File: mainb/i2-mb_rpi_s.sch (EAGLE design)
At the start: 30 parts, among them IC3 DS1307Z, T1 BC337, T2 BC337, X1 MICROMATCH-4, X15 C-GRID-03-70543, X2 MICROMATCH-4, X3 MICROMATCH-4, X8 MICROMATCH-4, X9 eth (mb->rpi)

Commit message: zmieniony ksztalt mainb
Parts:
- removed X1, X2, X3, X8: MICROMATCH-4, con-maritex:MICROMATCH-4
- removed X12, X13, X14: (no value), con-ptr500:AK500/3-H
- removed X4, X5, X6: (no value), con-ptr500:AK500/3
- added I2C_1, I2C_2, I2C_3, I2C_4: C-GRID-03-70553, con-molex:C-GRID-03-70553
- added PWR1, PWR2, PWR3: TBMP5103RC-KFV1, con-maritex:TBMP5103RC-KFV1
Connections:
- net +12V_OUT: now also PWR1-3.P, PWR2-3.P, PWR3-3.P; no longer X4-3.KL, X5-3.KL, X6-3.KL
- net +5V: now also PWR1-1.P, PWR2-1.P, PWR3-1.P; no longer X4-1.KL, X5-1.KL, X6-1.KL
- net GND: now also I2C_1-3.S, I2C_2-3.S, I2C_3-3.S, I2C_4-3.S, PWR1-2.P, PWR2-2.P, PWR3-2.P; no longer X1-4.S, X12-2.KL, X13-2.KL, X14-2.KL, X2-4.S, X3-4.S, X4-2.KL, X5-2.KL, X6-2.KL, X8-4.S
- net SCL: now also I2C_1-2.S, I2C_2-2.S, I2C_3-2.S, I2C_4-2.S; no longer X1-3.S, X2-3.S, X3-3.S, X8-3.S
- net SDA: now also I2C_1-1.S, I2C_2-1.S, I2C_3-1.S, I2C_4-1.S; no longer X1-2.S, X2-2.S, X3-2.S, X8-2.S

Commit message: 21.11.13 23:39
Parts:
- I2C_1: value C-GRID-03-70553 -> C-GRID-03-70543; device con-molex:C-GRID-03-70553 -> con-molex:C-GRID-03-70543; OC_FARNELL (none) -> unknown; OC_NEWARK (none) -> unknown
- renumbered X15 to PWR4
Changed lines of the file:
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@@
 <?xml version="1.0" encoding="utf-8"?>
 <!DOCTYPE eagle SYSTEM "eagle.dtd">
-<eagle version="6.4">
+<eagle version="6.1">
 <drawing>
 <settings>
@@
 <part name="SUPPLY2" library="supply2" deviceset="+5V/1" device="" value="+5V_RPI"/>
 <part name="SUPPLY3" library="supply2" deviceset="+5V/1" device="" value="+5V_RPI"/>
-<part name="X15" library="con-molex" deviceset="C-GRID-03" device="-70543"/>
+<part name="PWR4" library="con-molex" deviceset="C-GRID-03" device="-70543"/>
 <part name="SUPPLY1" library="supply2" deviceset="+12V" device="" value="+12V_OUT"/>
 <part name="GND1" library="supply1" deviceset="GND" device=""/>
 <part name="T1" library="transistor" deviceset="BC337" device=""/>
 <part name="T2" library="transistor" deviceset="BC337" device=""/>
-<part name="I2C_1" library="con-molex" deviceset="C-GRID-03" device="-70553"/>
 <part name="I2C_2" library="con-molex" deviceset="C-GRID-03" device="-70553"/>
 <part name="I2C_3" library="con-molex" deviceset="C-GRID-03" device="-70553"/>
@@
 <part name="PWR2" library="con-maritex" deviceset="TBMP5103RC-KF" device="V1"/>
 <part name="PWR3" library="con-maritex" deviceset="TBMP5103RC-KF" device="V1"/>
+<part name="I2C_1" library="con-molex" deviceset="C-GRID-03" device="-70543">
+<attribute name="MF" value=""/>
+<attribute name="MPN" value=""/>
+<attribute name="OC_FARNELL" value="unknown"/>
+<attribute name="OC_NEWARK" value="unknown"/>
+</part>
 </parts>
 <sheets>
@@
 <attribute name="VALUE" x="27.813" y="-44.831" size="1.778" layer="96"/>
 </instance>
-<instance part="X15" gate="-1" x="48.26" y="-2.54" smashed="yes" rot="R180">
+<instance part="PWR4" gate="-1" x="48.26" y="-2.54" smashed="yes" rot="R180">
 <attribute name="NAME" x="45.72" y="-1.778" size="1.524" layer="95" rot="R180"/>
 </instance>
-<instance part="X15" gate="-2" x="48.26" y="-15.24" rot="R180"/>
-<instance part="X15" gate="-3" x="48.26" y="25.4" rot="R180"/>
+<instance part="PWR4" gate="-2" x="48.26" y="-15.24" rot="R180"/>
+<instance part="PWR4" gate="-3" x="48.26" y="25.4" rot="R180"/>
 <instance part="SUPPLY1" gate="+12V" x="-63.5" y="25.4" smashed="yes">
 <attribute name="VALUE" x="-68.58" y="28.575" size="1.778" layer="96"/>
@@
 <instance part="T1" gate="G$1" x="-71.12" y="-12.7"/>
 <instance part="T2" gate="G$1" x="10.16" y="-15.24"/>
-<instance part="I2C_1" gate="-1" x="60.96" y="-55.88" smashed="yes">
-<attribute name="NAME" x="63.5" y="-56.642" size="1.524" layer="95"/>
-</instance>
-<instance part="I2C_1" gate="-2" x="60.96" y="-68.58"/>
-<instance part="I2C_1" gate="-3" x="60.96" y="-83.82"/>
 <instance part="I2C_2" gate="-1" x="60.96" y="-58.42" smashed="yes">
 <attribute name="NAME" x="63.5" y="-59.182" size="1.524" layer="95"/>
@@
 <instance part="PWR3" gate="-2" x="60.96" y="-22.86" rot="MR0"/>
 <instance part="PWR3" gate="-3" x="60.96" y="27.94" rot="MR0"/>
+<instance part="I2C_1" gate="-1" x="60.96" y="-55.88" smashed="yes">
+<attribute name="NAME" x="63.5" y="-56.642" size="1.524" layer="95"/>
+</instance>
+<instance part="I2C_1" gate="-2" x="60.96" y="-68.58"/>
+<instance part="I2C_1" gate="-3" x="60.96" y="-83.82"/>
 </instances>
 <busses>
@@
 <junction x="55.88" y="-73.66"/>
 <label x="49.53" y="-68.326" size="1.778" layer="95"/>
-<pinref part="I2C_1" gate="-2" pin="S"/>
 <pinref part="I2C_2" gate="-2" pin="S"/>
 <pinref part="I2C_3" gate="-2" pin="S"/>
 <pinref part="I2C_4" gate="-2" pin="S"/>
+<pinref part="I2C_1" gate="-2" pin="S"/>
 </segment>
 <segment>
@@
 <junction x="55.88" y="-60.96"/>
 <label x="49.276" y="-55.626" size="1.778" layer="95"/>
-<pinref part="I2C_1" gate="-1" pin="S"/>
 <pinref part="I2C_2" gate="-1" pin="S"/>
 <pinref part="I2C_3" gate="-1" pin="S"/>
 <pinref part="I2C_4" gate="-1" pin="S"/>
+<pinref part="I2C_1" gate="-1" pin="S"/>
 </segment>
 <segment>
@@
 <pinref part="SUPPLY7" gate="+5V" pin="+5V"/>
 <wire x1="53.34" y1="7.62" x2="53.34" y2="5.08" width="0.1524" layer="91"/>
-<pinref part="X15" gate="-1" pin="S"/>
+<pinref part="PWR4" gate="-1" pin="S"/>
 <wire x1="53.34" y1="5.08" x2="53.34" y2="2.54" width="0.1524" layer="91"/>
 <wire x1="53.34" y1="2.54" x2="53.34" y2="0" width="0.1524" layer="91"/>
@@
 <segment>
 <pinref part="GND11" gate="1" pin="GND"/>
-<pinref part="X15" gate="-2" pin="S"/>
+<pinref part="PWR4" gate="-2" pin="S"/>
 <wire x1="50.8" y1="-15.24" x2="53.34" y2="-15.24" width="0.1524" layer="91"/>
 <wire x1="53.34" y1="-15.24" x2="53.34" y2="-17.78" width="0.1524" layer="91"/>
@@
 <junction x="55.88" y="-88.9"/>
 <junction x="55.88" y="-91.44"/>
-<pinref part="I2C_1" gate="-3" pin="S"/>
 <pinref part="I2C_2" gate="-3" pin="S"/>
 <pinref part="I2C_3" gate="-3" pin="S"/>
 <pinref part="I2C_4" gate="-3" pin="S"/>
+<pinref part="I2C_1" gate="-3" pin="S"/>
 </segment>
 <segment>
@@
 <pinref part="SUPPLY6" gate="+12V" pin="+12V"/>
 <wire x1="53.34" y1="35.56" x2="53.34" y2="33.02" width="0.1524" layer="91"/>
-<pinref part="X15" gate="-3" pin="S"/>
+<pinref part="PWR4" gate="-3" pin="S"/>
 <wire x1="53.34" y1="33.02" x2="53.34" y2="30.48" width="0.1524" layer="91"/>
 <wire x1="53.34" y1="30.48" x2="53.34" y2="27.94" width="0.1524" layer="91"/>

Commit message: 26.11 10:46
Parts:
- added C1: 100n, rcl:C-EUC0603
- added LED1, LED2, LED3: LED0603, wb:LED0603
- added R4, R5, R6: 500, rcl:R-EU_R0603
- added R7: (no value), rcl:R-EU_R0603
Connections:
- new net LED2: LED2.C, U$2.GPIO23
- new net LED3: LED3.C, U$2.GPIO24
- new net N$10: IC3.SQW, R7.2
- new net N$4: LED2.A, R5.1
- new net N$5: LED1.A, R4.1
- new net N$7: LED1.C, U$2.GPIO25
- new net N$8: LED3.A, R6.1
- net +5V_RPI: now also C1.1, R4.2, R5.2, R6.2, R7.1
- net GND: now also C1.2
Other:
- note removed: "AKU-"
- moved on the sheet: BAT, I2C_1-1, I2C_1-2, I2C_1-3, I2C_2-1, I2C_2-2, I2C_2-3, I2C_3-1, I2C_3-2, I2C_3-3, I2C_4-1, I2C_4-2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

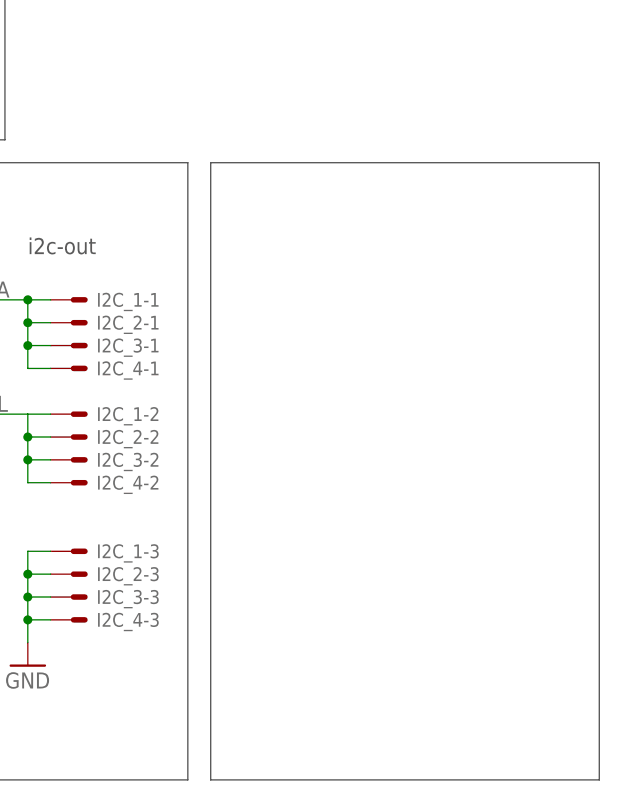
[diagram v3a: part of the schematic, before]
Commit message: RPi camera board added and library, added servos.lbr
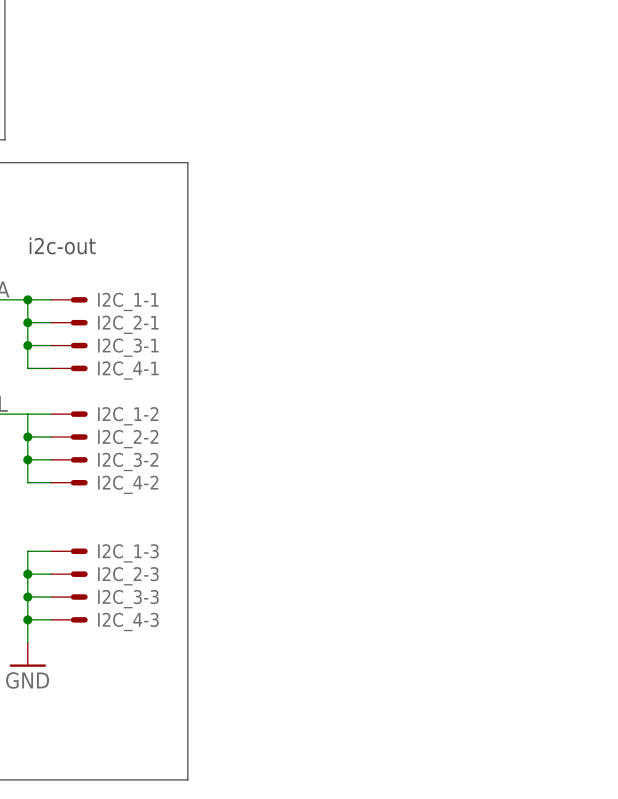
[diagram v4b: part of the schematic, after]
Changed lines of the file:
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@@
 <circle x="-157.48" y="-10.16" radius="2.54" width="1.4224" layer="94"/>
 <text x="-170.18" y="-10.16" size="2.54" layer="97">AKU+</text>
-<wire x1="96.52" y1="-109.22" x2="96.52" y2="-40.64" width="0.1524" layer="97"/>
-<wire x1="139.7" y1="-109.22" x2="139.7" y2="-40.64" width="0.1524" layer="97"/>
-<wire x1="96.52" y1="-109.22" x2="139.7" y2="-109.22" width="0.1524" layer="97"/>
-<wire x1="96.52" y1="-40.64" x2="139.7" y2="-40.64" width="0.1524" layer="97"/>
 </plain>
 <instances>

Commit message: 03-12-13 20:52
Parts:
- I2C_1: value C-GRID-03-70543 -> MICROMATCH-4; device con-molex:C-GRID-03-70543 -> con-amp-micromatch:MICROMATCH-4; OC_FARNELL unknown -> (none); OC_NEWARK unknown -> (none)
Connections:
- net +5V: now also I2C_1-4.S
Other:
- moved on the sheet: R28, R3, T1, T2, U$8, X9-1, X9-2, X9-3, X9-4, X9-5, X9-6, X9-7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

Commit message: 11.12.13 18:50
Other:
- note removed: "i2c-out"
- moved on the sheet: BAT, I2C_1-1, I2C_1-2, I2C_1-3, I2C_1-4, I2C_2-1, I2C_2-2, I2C_2-3, I2C_3-1, I2C_3-2, I2C_3-3, I2C_4-1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

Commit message: misc changes
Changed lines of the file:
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@@
 <?xml version="1.0" encoding="utf-8"?>
 <!DOCTYPE eagle SYSTEM "eagle.dtd">
-<eagle version="6.1">
+<eagle version="6.4">
 <drawing>
 <settings>
@@
 <part name="I2C_1" library="con-amp-micromatch" deviceset="MICROMATCH-4" device=""/>
 <part name="SUPPLY5" library="supply2" deviceset="+5V" device="" value="+5V_OUT"/>
+<part name="GND1" library="supply1" deviceset="GND" device=""/>
 </parts>
 <sheets>
@@
 <attribute name="VALUE" x="41.275" y="3.175" size="1.778" layer="96"/>
 </instance>
+<instance part="GND1" gate="1" x="40.64" y="-38.1"/>
 </instances>
 <busses>
@@
 <wire x1="-38.1" y1="-40.64" x2="-38.1" y2="-106.68" width="0.762" layer="92"/>
 <wire x1="12.7" y1="5.08" x2="12.7" y2="-40.64" width="0.762" layer="92"/>
-<wire x1="-38.1" y1="-106.68" x2="-12.7" y2="-106.68" width="0.762" layer="92"/>
+<wire x1="-38.1" y1="-106.68" x2="-17.78" y2="-106.68" width="0.762" layer="92"/>
 </segment>
 </bus>
@@
 </segment>
 <segment>
+<pinref part="I2C_4" gate="-2" pin="S"/>
+<wire x1="-20.32" y1="-119.38" x2="-20.32" y2="-106.68" width="0.1524" layer="91"/>
+</segment>
+<segment>
 <wire x1="12.7" y1="-5.08" x2="15.24" y2="-7.62" width="0.1524" layer="91"/>
 <wire x1="15.24" y1="-7.62" x2="38.1" y2="-7.62" width="0.1524" layer="91"/>
 <wire x1="38.1" y1="-7.62" x2="45.72" y2="-7.62" width="0.1524" layer="91"/>
-<wire x1="-20.32" y1="-119.38" x2="-20.32" y2="-111.76" width="0.1524" layer="91"/>
-<wire x1="-20.32" y1="-111.76" x2="38.1" y2="-30.48" width="0.1524" layer="91"/>
 <wire x1="38.1" y1="-30.48" x2="38.1" y2="-20.32" width="0.1524" layer="91"/>
 <wire x1="38.1" y1="-20.32" x2="38.1" y2="-7.62" width="0.1524" layer="91"/>
@@
 <wire x1="45.72" y1="-20.32" x2="38.1" y2="-20.32" width="0.1524" layer="91"/>
 <junction x="38.1" y="-20.32"/>
-<junction x="38.1" y="-30.48"/>
 <label x="21.59" y="-7.366" size="1.778" layer="95"/>
 <pinref part="I2C_2" gate="-2" pin="S"/>
 <pinref part="I2C_3" gate="-2" pin="S"/>
-<pinref part="I2C_4" gate="-2" pin="S"/>
 <pinref part="I2C_1" gate="-2" pin="S"/>
 </segment>
@@
 </segment>
 <segment>
+<pinref part="I2C_4" gate="-1" pin="S"/>
+<wire x1="-17.78" y1="-119.38" x2="-17.78" y2="-106.68" width="0.1524" layer="91"/>
+</segment>
+<segment>
 <wire x1="12.7" y1="-2.54" x2="15.24" y2="-5.08" width="0.1524" layer="91"/>
 <wire x1="15.24" y1="-5.08" x2="35.56" y2="-5.08" width="0.1524" layer="91"/>
 <wire x1="35.56" y1="-5.08" x2="45.72" y2="-5.08" width="0.1524" layer="91"/>
-<wire x1="-17.78" y1="-119.38" x2="-17.78" y2="-109.22" width="0.1524" layer="91"/>
 <wire x1="45.72" y1="-27.94" x2="35.56" y2="-27.94" width="0.1524" layer="91"/>
-<wire x1="-17.78" y1="-109.22" x2="35.56" y2="-27.94" width="0.1524" layer="91"/>
 <wire x1="45.72" y1="-17.78" x2="35.56" y2="-17.78" width="0.1524" layer="91"/>
 <wire x1="35.56" y1="-27.94" x2="35.56" y2="-17.78" width="0.1524" layer="91"/>
@@
 <junction x="35.56" y="-5.08"/>
 <junction x="35.56" y="-17.78"/>
-<junction x="35.56" y="-27.94"/>
 <label x="21.336" y="-4.826" size="1.778" layer="95"/>
 <pinref part="I2C_2" gate="-1" pin="S"/>
 <pinref part="I2C_3" gate="-1" pin="S"/>
-<pinref part="I2C_4" gate="-1" pin="S"/>
 <pinref part="I2C_1" gate="-1" pin="S"/>
 </segment>
@@
 </segment>
 <segment>
-<wire x1="45.72" y1="-33.02" x2="40.64" y2="-33.02" width="0.1524" layer="91"/>
-<wire x1="45.72" y1="-10.16" x2="40.64" y2="-10.16" width="0.1524" layer="91"/>
-<wire x1="40.64" y1="-10.16" x2="40.64" y2="-22.86" width="0.1524" layer="91"/>
-<wire x1="40.64" y1="-22.86" x2="40.64" y2="-33.02" width="0.1524" layer="91"/>
+<pinref part="GND12" gate="1" pin="GND"/>
+<pinref part="I2C_4" gate="-3" pin="S"/>
 <wire x1="-22.86" y1="-119.38" x2="-22.86" y2="-114.3" width="0.1524" layer="91"/>
-<wire x1="40.64" y1="-33.02" x2="-22.86" y2="-114.3" width="0.1524" layer="91"/>
-<pinref part="GND12" gate="1" pin="GND"/>
 <wire x1="-22.86" y1="-114.3" x2="-27.94" y2="-114.3" width="0.1524" layer="91"/>
-<wire x1="45.72" y1="-22.86" x2="40.64" y2="-22.86" width="0.1524" layer="91"/>
-<junction x="40.64" y="-22.86"/>
-<junction x="40.64" y="-33.02"/>
-<junction x="-22.86" y="-114.3"/>
-<pinref part="I2C_2" gate="-3" pin="S"/>
-<pinref part="I2C_3" gate="-3" pin="S"/>
-<pinref part="I2C_4" gate="-3" pin="S"/>
-<pinref part="I2C_1" gate="-3" pin="S"/>
 </segment>
 <segment>
@@
 <pinref part="GND14" gate="1" pin="GND"/>
 </segment>
-</net>
+<segment>
+<wire x1="45.72" y1="-33.02" x2="40.64" y2="-33.02" width="0.1524" layer="91"/>
+<wire x1="45.72" y1="-10.16" x2="40.64" y2="-10.16" width="0.1524" layer="91"/>
+<wire x1="40.64" y1="-10.16" x2="40.64" y2="-22.86" width="0.1524" layer="91"/>
+<wire x1="40.64" y1="-22.86" x2="40.64" y2="-33.02" width="0.1524" layer="91"/>
+<wire x1="45.72" y1="-22.86" x2="40.64" y2="-22.86" width="0.1524" layer="91"/>
+<junction x="40.64" y="-22.86"/>
+<pinref part="I2C_2" gate="-3" pin="S"/>
+<pinref part="I2C_3" gate="-3" pin="S"/>
+<pinref part="I2C_1" gate="-3" pin="S"/>
+<pinref part="GND1" gate="1" pin="GND"/>
+<wire x1="40.64" y1="-33.02" x2="40.64" y2="-35.56" width="0.1524" layer="91"/>
+<junction x="40.64" y="-33.02"/>
+</segment>
+</net>

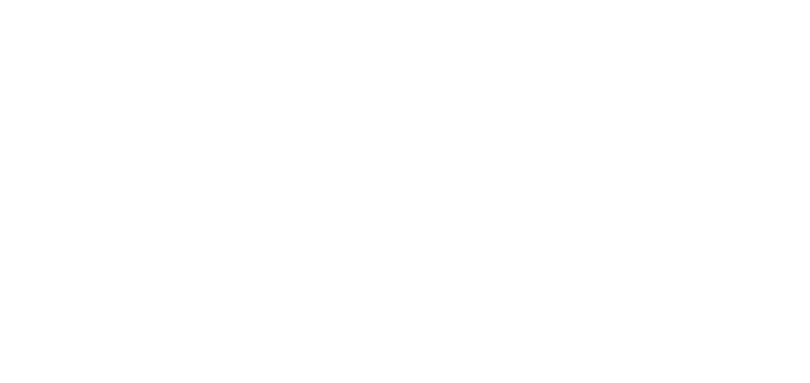
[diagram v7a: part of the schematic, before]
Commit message: /mainb: 1) pins on relays
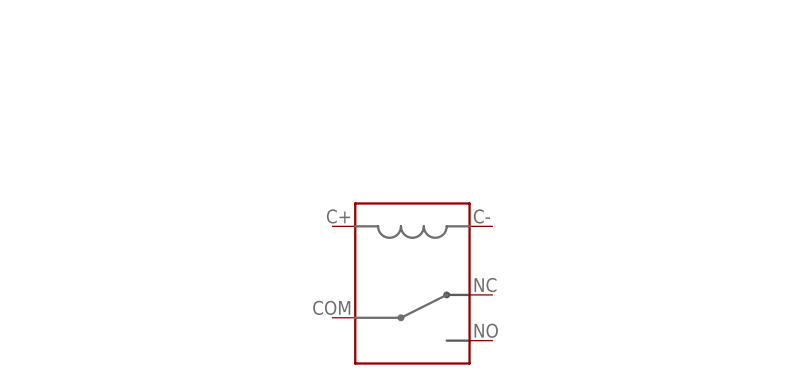
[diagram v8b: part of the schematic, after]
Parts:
- added U$9: FBR51, wb:FBR51
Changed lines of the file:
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@@
 <?xml version="1.0" encoding="utf-8"?>
 <!DOCTYPE eagle SYSTEM "eagle.dtd">
-<eagle version="6.4">
+<eagle version="6.5.0">
 <drawing>
 <settings>
@@
 <part name="SUPPLY5" library="supply2" deviceset="+5V" device="" value="+5V_OUT"/>
 <part name="GND1" library="supply1" deviceset="GND" device=""/>
+<part name="U$9" library="wb" deviceset="FBR51" device=""/>
 </parts>
 <sheets>
@@
 </instance>
 <instance part="GND1" gate="1" x="40.64" y="-38.1"/>
+<instance part="U$9" gate="G$1" x="-187.96" y="-144.78"/>
 </instances>
 <busses>
